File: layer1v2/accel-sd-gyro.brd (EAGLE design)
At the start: 17.8 x 49.5 mm, 17 parts, among them IC2 LGD20H, U1 MMA8452Q, U2 microSD

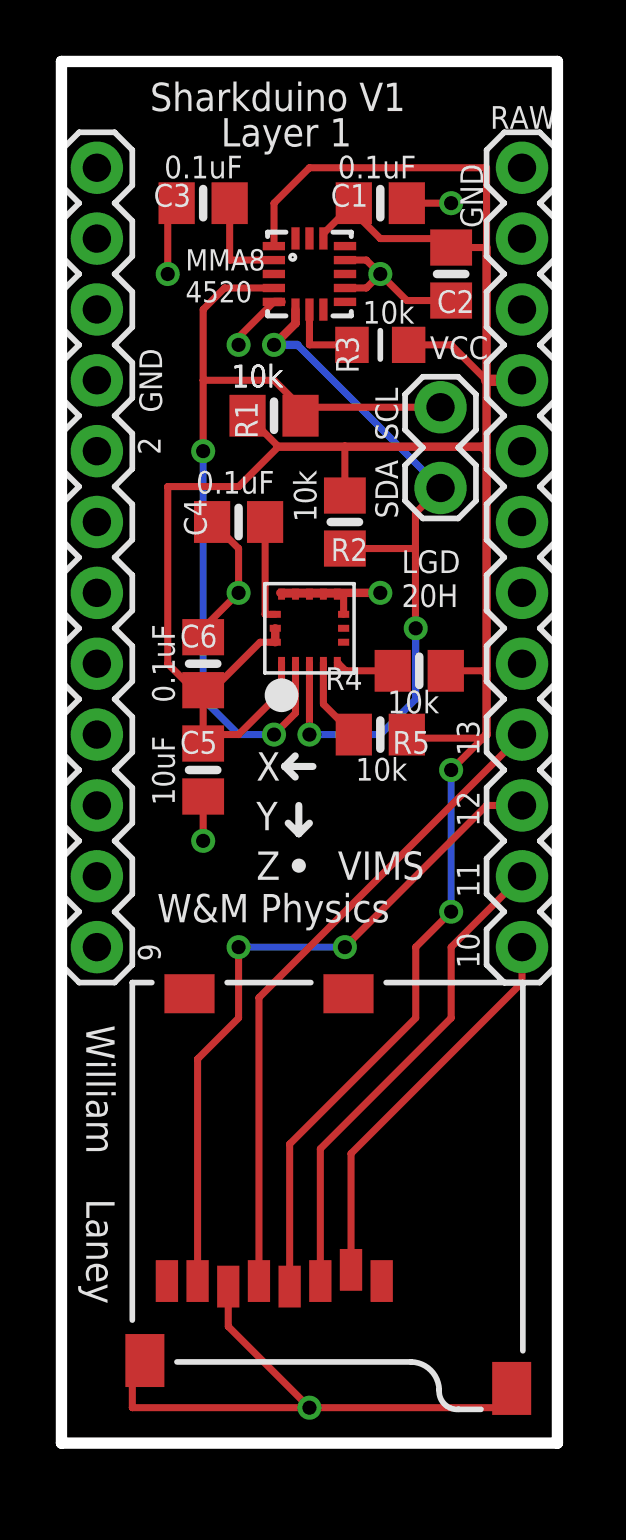
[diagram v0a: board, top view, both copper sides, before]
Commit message: extned layer 1 length to fit uSD
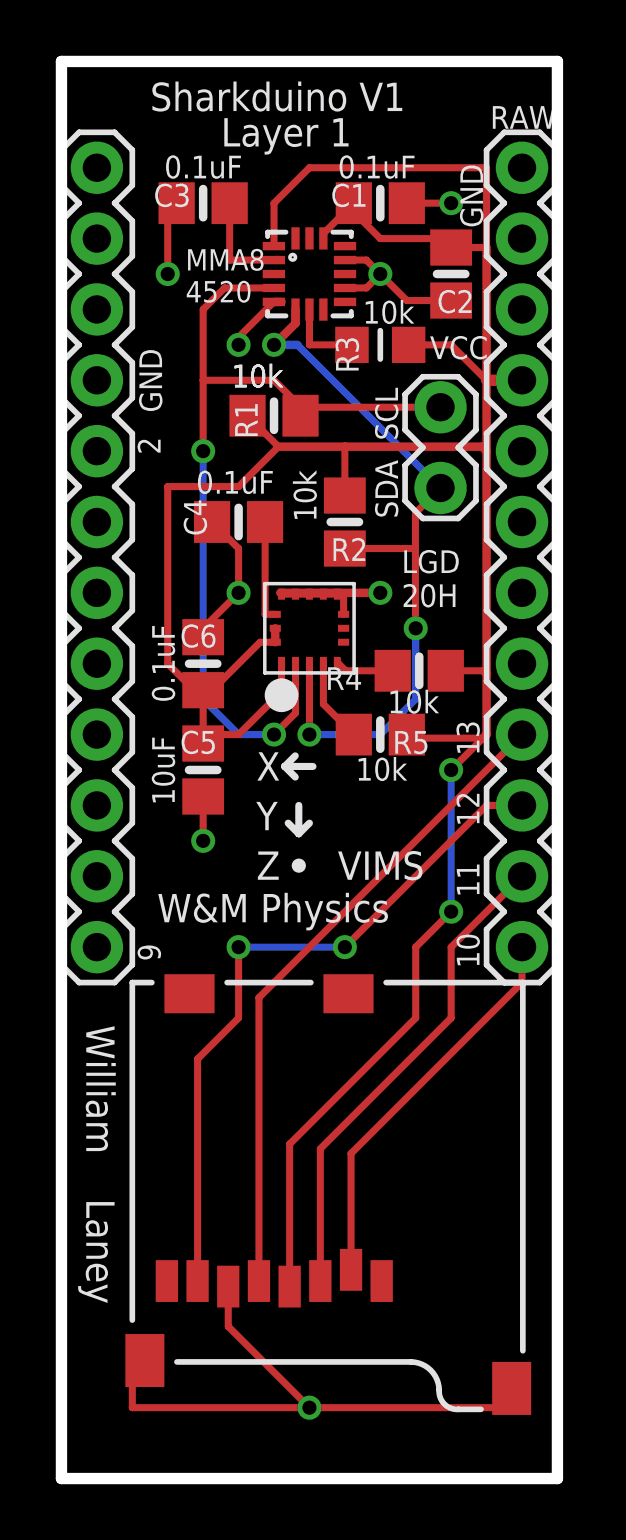
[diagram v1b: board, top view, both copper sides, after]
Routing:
- removed copper zone on layer 16, net GND
- removed copper zone on layer 1, net N$7
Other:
- board size 17.8 x 49.5 mm -> 17.8 x 50.8 mm
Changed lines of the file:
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@@
 <board>
 <plain>
-<wire x1="0" y1="0" x2="0" y2="49.53" width="0.4064" layer="20"/>
 <wire x1="0" y1="49.53" x2="17.78" y2="49.53" width="0.4064" layer="20"/>
-<wire x1="17.78" y1="49.53" x2="17.78" y2="0" width="0.4064" layer="20"/>
-<wire x1="0" y1="0" x2="17.78" y2="0" width="0.4064" layer="20"/>
 <wire x1="8.509" y1="21.844" x2="8.509" y2="22.86" width="0.254" layer="21"/>
 <wire x1="8.509" y1="21.844" x2="8.89" y2="22.225" width="0.254" layer="21"/>
@@
 <text x="5.715" y="45.339" size="1.016" layer="22" font="vector" ratio="15" rot="MR270">Shankduino V1 Layer 1</text>
 <text x="10.795" y="45.085" size="1.016" layer="22" font="vector" ratio="15" rot="MR270">welaney@email.wm.edu</text>
+<wire x1="0" y1="49.53" x2="0" y2="-1.27" width="0.4064" layer="20"/>
+<wire x1="0" y1="-1.27" x2="17.78" y2="-1.27" width="0.4064" layer="20"/>
+<wire x1="17.78" y1="-1.27" x2="17.78" y2="49.53" width="0.4064" layer="20"/>
 </plain>
 <attributes>
@@
 <contactref element="J2" pad="2"/>
 <via x="8.89" y="1.27" extent="1-16" drill="0.508"/>
-<polygon width="0.254" layer="16" isolate="0.3048">
-<vertex x="0" y="49.53"/>
-<vertex x="17.78" y="49.53"/>
-<vertex x="17.78" y="0"/>
-<vertex x="0" y="0"/>
-</polygon>
 <wire x1="5.98" y1="5.61" x2="5.98" y2="4.18" width="0.254" layer="1"/>
 <wire x1="5.98" y1="4.18" x2="8.89" y2="1.27" width="0.254" layer="1"/>
@@
 <signal name="N$6">
 </signal>
-<signal name="N$7">
-<polygon width="0.254" layer="1" isolate="0.3048">
-<vertex x="0" y="49.53"/>
-<vertex x="0" y="0"/>
-<vertex x="17.78" y="0"/>
-<vertex x="17.78" y="49.53"/>
-</polygon>
-</signal>
 <signal name="N$8">

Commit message: silk screen changes, added top ground pour, updated doc
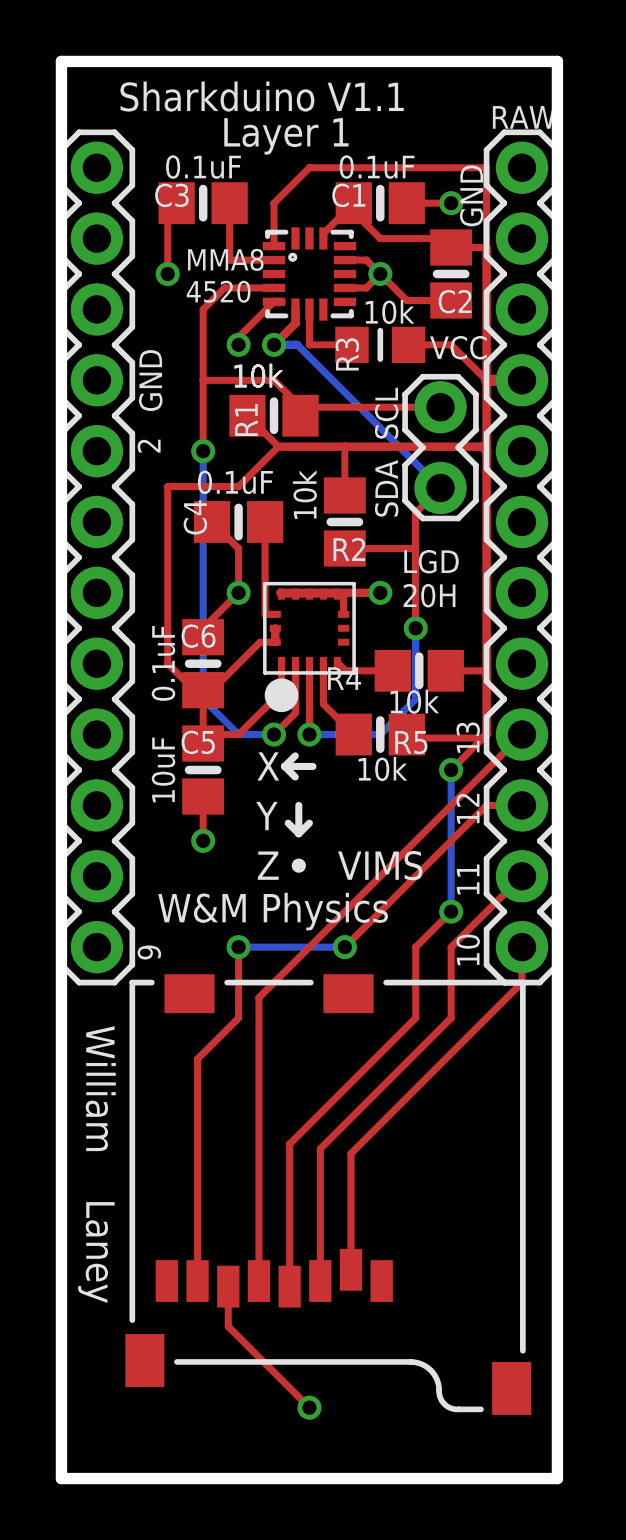
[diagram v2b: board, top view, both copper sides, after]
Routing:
- net GND: track 47.9 -> 32.6 mm
- added copper zone on layer 1, net GND
- added copper zone on layer 16, net GND
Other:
- board text added: "Sharkduino V1.1"
- board text added: "Sharkduino V1.1 Layer 1"
- board text removed: "Shankduino V1 Layer 1"
- board text removed: "Sharkduino V1"
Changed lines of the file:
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@@
 <setting verticaltext="up"/>
 </settings>
-<grid distance="0.05" unitdist="inch" unit="inch" style="lines" multiple="1" display="yes" altdistance="0.005" altunitdist="inch" altunit="inch"/>
+<grid distance="0.05" unitdist="inch" unit="inch" style="lines" multiple="1" display="yes" altdistance="0.025" altunitdist="inch" altunit="inch"/>
 <layers>
 <layer number="1" name="Top" color="4" fill="1" visible="yes" active="yes"/>
@@
 <text x="0.889" y="14.986" size="1.016" layer="21" font="vector" ratio="15" rot="SR270">William</text>
 <text x="0.889" y="8.763" size="1.016" layer="21" font="vector" ratio="15" rot="SR270">Laney</text>
-<text x="3.175" y="47.752" size="1.016" layer="21" font="vector" ratio="15">Sharkduino V1</text>
+<text x="2.032" y="47.752" size="1.016" layer="21" font="vector" ratio="15">Sharkduino V1.1</text>
 <text x="5.715" y="46.482" size="1.016" layer="21" font="vector" ratio="15">Layer 1</text>
 <text x="3.556" y="35.433" size="0.8128" layer="21" font="vector" ratio="15" rot="R90">2</text>
@@
 <text x="1.397" y="13.462" size="1.016" layer="22" font="vector" ratio="15" rot="MR180">William Laney 2016</text>
 <text x="0.762" y="10.287" size="1.016" layer="22" font="vector" ratio="15" rot="MR180">W&amp;M Physics   VIMS</text>
-<text x="5.715" y="45.339" size="1.016" layer="22" font="vector" ratio="15" rot="MR270">Shankduino V1 Layer 1</text>
+<text x="5.715" y="45.339" size="1.016" layer="22" font="vector" ratio="15" rot="MR270">Sharkduino V1.1 Layer 1</text>
 <text x="10.795" y="45.085" size="1.016" layer="22" font="vector" ratio="15" rot="MR270">welaney@email.wm.edu</text>
 <wire x1="0" y1="49.53" x2="0" y2="-1.27" width="0.4064" layer="20"/>
@@
 <wire x1="5.98" y1="4.18" x2="8.89" y2="1.27" width="0.254" layer="1"/>
 <wire x1="2.99" y1="2.96" x2="2.54" y2="2.96" width="0.254" layer="1"/>
-<wire x1="2.54" y1="2.96" x2="2.54" y2="1.27" width="0.254" layer="1"/>
-<wire x1="2.54" y1="1.27" x2="8.89" y2="1.27" width="0.254" layer="1"/>
-<wire x1="8.89" y1="1.27" x2="16.14" y2="1.27" width="0.254" layer="1"/>
 <wire x1="16.14" y1="1.27" x2="16.14" y2="1.96" width="0.254" layer="1"/>
 <contactref element="C4" pad="1"/>
@@
 <via x="11.43" y="30.48" extent="1-16" drill="0.508"/>
 <wire x1="13.97" y1="40.96" x2="12.38" y2="40.96" width="0.254" layer="1"/>
+<polygon width="0.254" layer="16" isolate="0.3048">
+<vertex x="0" y="49.53"/>
+<vertex x="17.78" y="49.53"/>
+<vertex x="17.78" y="-1.27"/>
+<vertex x="0" y="-1.27"/>
+</polygon>
+<polygon width="0.254" layer="1" isolate="0.3048">
+<vertex x="0" y="49.53"/>
+<vertex x="17.78" y="49.53"/>
+<vertex x="17.78" y="-1.27"/>
+<vertex x="0" y="-1.27"/>
+</polygon>
 </signal>
 <signal name="SCL">
